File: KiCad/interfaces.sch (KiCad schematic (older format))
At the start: 24 parts, among them J3 SI-51005-F

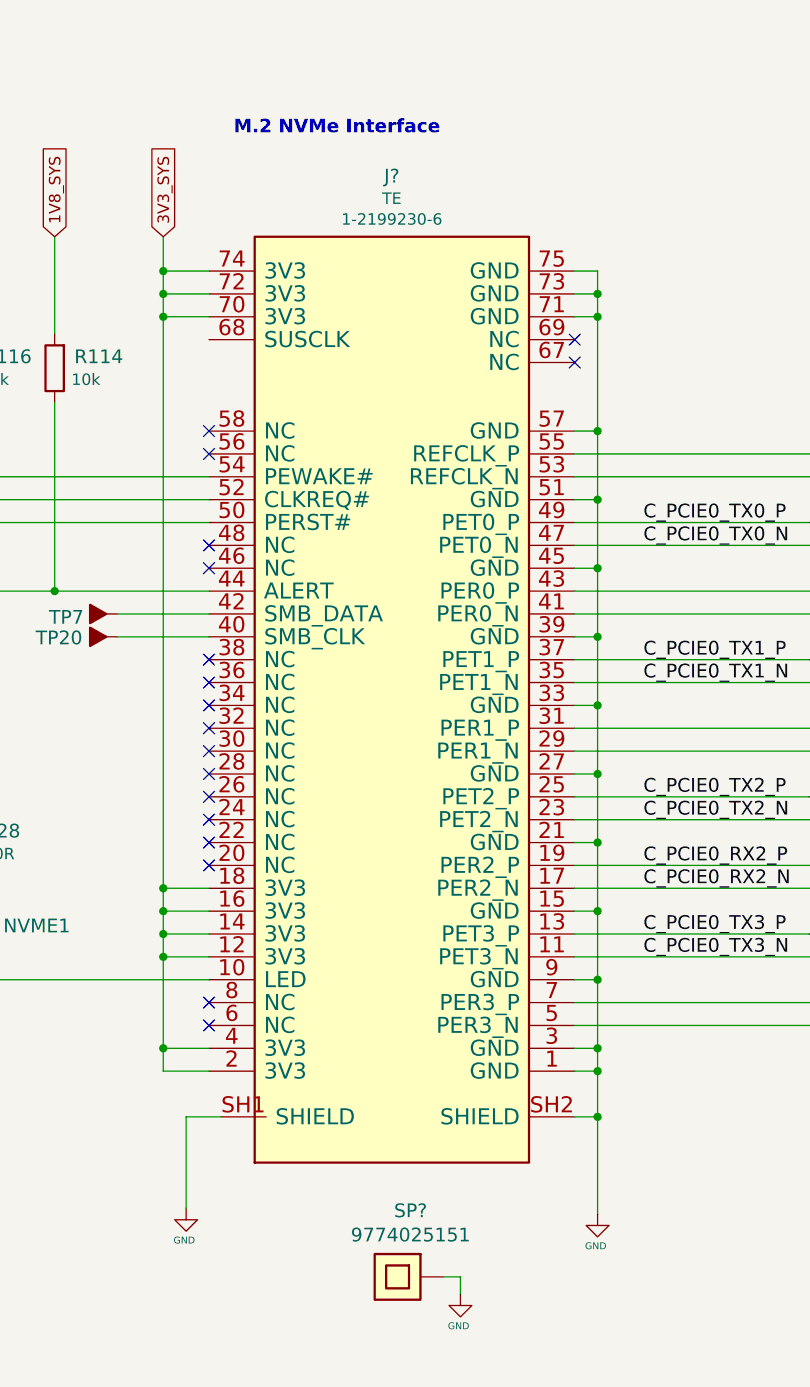
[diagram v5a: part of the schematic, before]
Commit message: Annotate parts
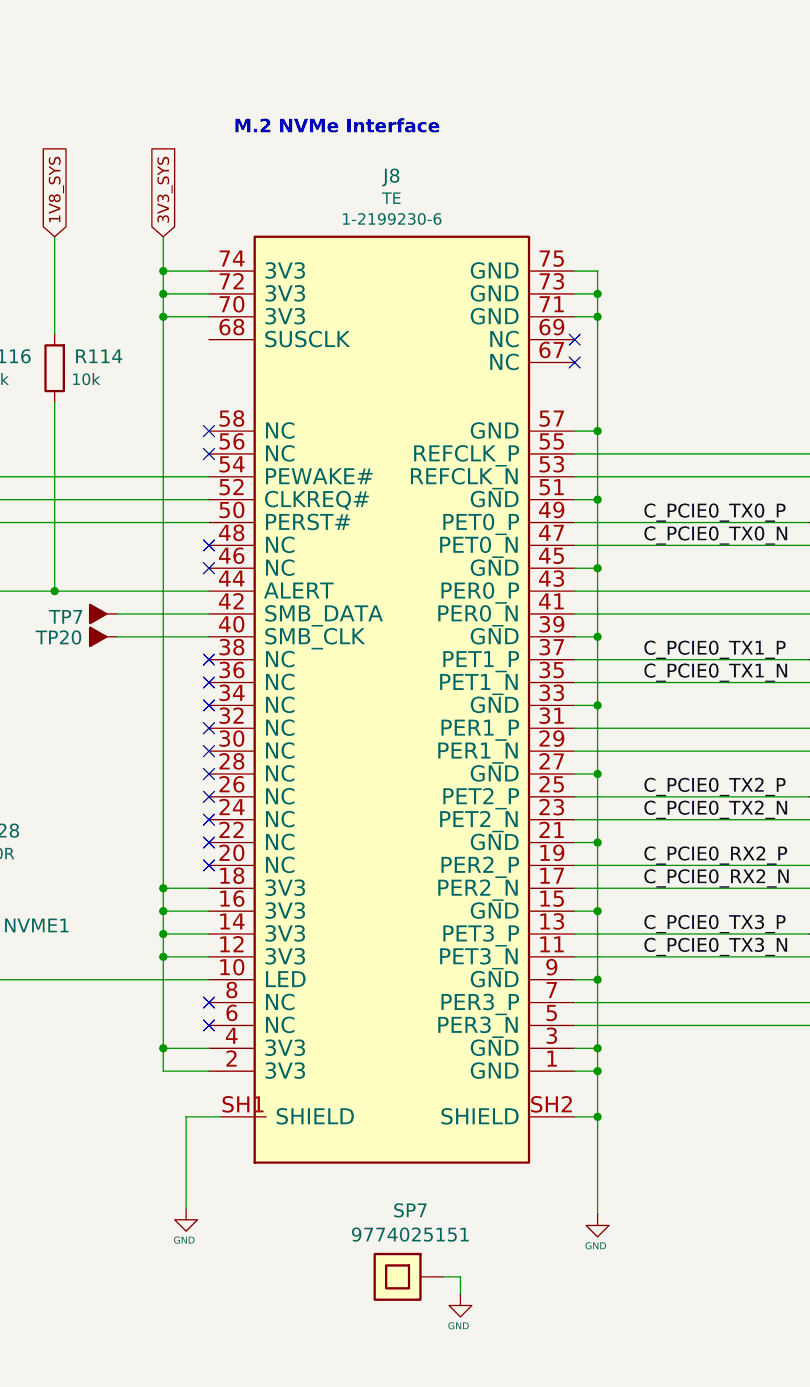
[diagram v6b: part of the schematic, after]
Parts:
- gave numbers to parts that had none: 2
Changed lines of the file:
@@
 3V3_SYS
 $Comp
-L antmicroPciConnectors:1-2199230-6 J?
+L antmicroPciConnectors:1-2199230-6 J8
 U 1 1 6246454E
 P 5475 7150
-F 0 "J?" H 5475 9815 60  0000 C CNN
+F 0 "J8" H 5475 9815 60  0000 C CNN
 F 1 "1-2199230-6" H 5325 5450 60  0001 C CNN
 F 2 "antmicro-footprints:1-2199230-6" H 5325 5450 60  0001 C CNN
@@
 $EndComp
 $Comp
-L antmicroMechanicalParts:9774025151 SP?
+L antmicroMechanicalParts:9774025151 SP7
 U 1 1 6248F20F
 P 5500 9300
-F 0 "SP?" H 5443 9011 60  0000 C CNN
+F 0 "SP7" H 5443 9011 60  0000 C CNN
 F 1 "9774025151" H 5443 9117 60  0000 C CNN
 F 2 "antmicro-footprints:9774025151" H 5500 9300 60  0001 C CNN

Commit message: Update Ethernet symbol and footprint
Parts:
- removed J3: SI-51005-F, jetson-nano-baseboard-footprints:SI-51005-F, symbol jetson-nano-baseboard:SI-51005-F
- added J3: SI-51005-F, antmicro-footprints:SI-51005-F, symbol antmicroModularConnectorsJacksWithMagnetics:SI-51005-F
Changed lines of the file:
@@
 Wire Wire Line
 	7600 7800 8400 7800
-$Comp
-L jetson-nano-baseboard:SI-51005-F J3
-U 1 1 61B50EDA
-P 12525 6200
-F 0 "J3" H 12525 7565 60  0000 C CNN
-F 1 "SI-51005-F" H 12525 7383 60  0001 C CNN
-F 2 "jetson-nano-baseboard-footprints:SI-51005-F" H 12525 5250 60  0001 C CNN
-F 3 "https://belfuse.com/resources/drawings/magneticsolutions/dr-mag-si-51005-fb.pdf" H 12525 6200 60  0001 C CNN
-F 4 "Bel Magnetic Solutions " H 12525 7467 50  0000 C CNN "Manufacturer"
-F 5 "SI-51005-F " H 12525 7376 50  0000 C CNN "MPN"
-	1    12525 6200
-	1    0    0    -1
-$EndComp
 Wire Wire Line
 	11375 5300 11225 5300
@@
 	-1   0    0    1
 $EndComp
+$Comp
+L antmicroModularConnectorsJacksWithMagnetics:SI-51005-F J3
+U 1 1 61D7A49A
+P 12525 6200
+F 0 "J3" H 12525 7489 60  0000 C CNN
+F 1 "SI-51005-F" H 12525 7383 60  0000 C CNN
+F 2 "antmicro-footprints:SI-51005-F" H 12525 5250 60  0001 C CNN
+F 3 "https://belfuse.com/resources/drawings/magneticsolutions/dr-mag-si-51005-fb.pdf" H 12525 6200 60  0001 C CNN
+F 4 "Bel Magnetic Solutions " H 12525 6200 50  0001 C CNN "Manufacturer"
+F 5 "SI-51005-F " H 12525 6200 50  0001 C CNN "MPN"
+	1    12525 6200
+	1    0    0    -1
+$EndComp
 $EndSCHEMATC

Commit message: Saving changes for later work
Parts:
- removed J3: SI-51005-F, antmicro-footprints:SI-51005-F, symbol antmicroModularConnectorsJacksWithMagnetics:SI-51005-F
- added J10: 5-2337992-8, antmicro-footprints:5-2337992-8, symbol antmicroModularConnectorsJacksWithMagnetics:5-2337992-8
- added J2: DF17(4.0)-50DS-0.5V(57), antmicro-footprints:HRS_DF17(4.0)-50DS-0.5V(57), symbol antmicroRectangularConnectorsHeadersMalePins:DF17(4.0)-50DS-0.5V(57)
- added J3: L834-1G1T-S7, antmicro-footprints:BEL_L834-1G1T-S7, symbol antmicroModularConnectorsJacksWithMagnetics:L834-1G1T-S7
- added T8: WE-RJ45_7499511611A, antmicro-footprints:7499511611A, symbol antmicroModularConnectorsJacksWithMagnetics:WE-RJ45_7499511611A
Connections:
- net labels added: CAN_RX, CAN_TX, DP_HDP, EDP0_TX_N, EDP0_TX_P, EDP1_TX_N, EDP1_TX_P, EDP2_TX_N, EDP2_TX_P, EDP3_TX_N, EDP3_TX_P, EDP_AUX_N, EDP_AUX_P, I2C1_SCL, I2C1_SDA, PCIE1_CLKREQ, PCIE1_CLK_N, PCIE1_CLK_P, PCIE1_RST, PCIE1_RX0_N, PCIE1_RX0_P, PCIE1_TX0_N, PCIE1_TX0_P, SPI0_CS#, SPI0_MISO, SPI0_MOSI, SPI0_SCK, UART1_RX, UART1_TX, USB2_D_N, USB2_D_P, VIN
- wire segments 126 -> 195
